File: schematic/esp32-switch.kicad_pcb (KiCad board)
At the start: 2 copper layers, 80 x 100 mm, 28 parts, among them J1 Direction, J11 Bouton 5v, J17 Bouton Batterie, J2 + - home, J3 a b x y, J4 L R ZL ZR, J5 Joy D, J6 Joy G, J7 Moteur vibration, Q1 BC547, U1 ESP32-DevKitC

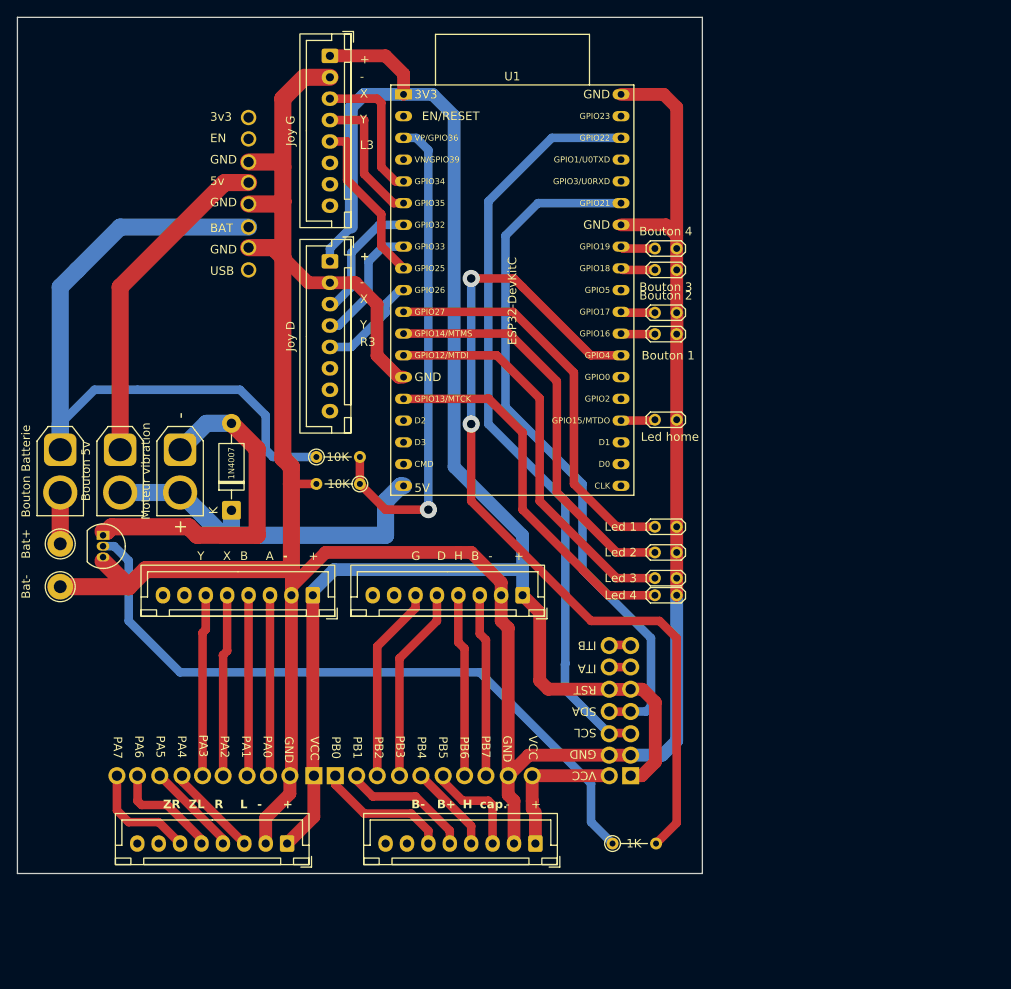
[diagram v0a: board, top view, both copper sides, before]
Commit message: changment des pates des leds
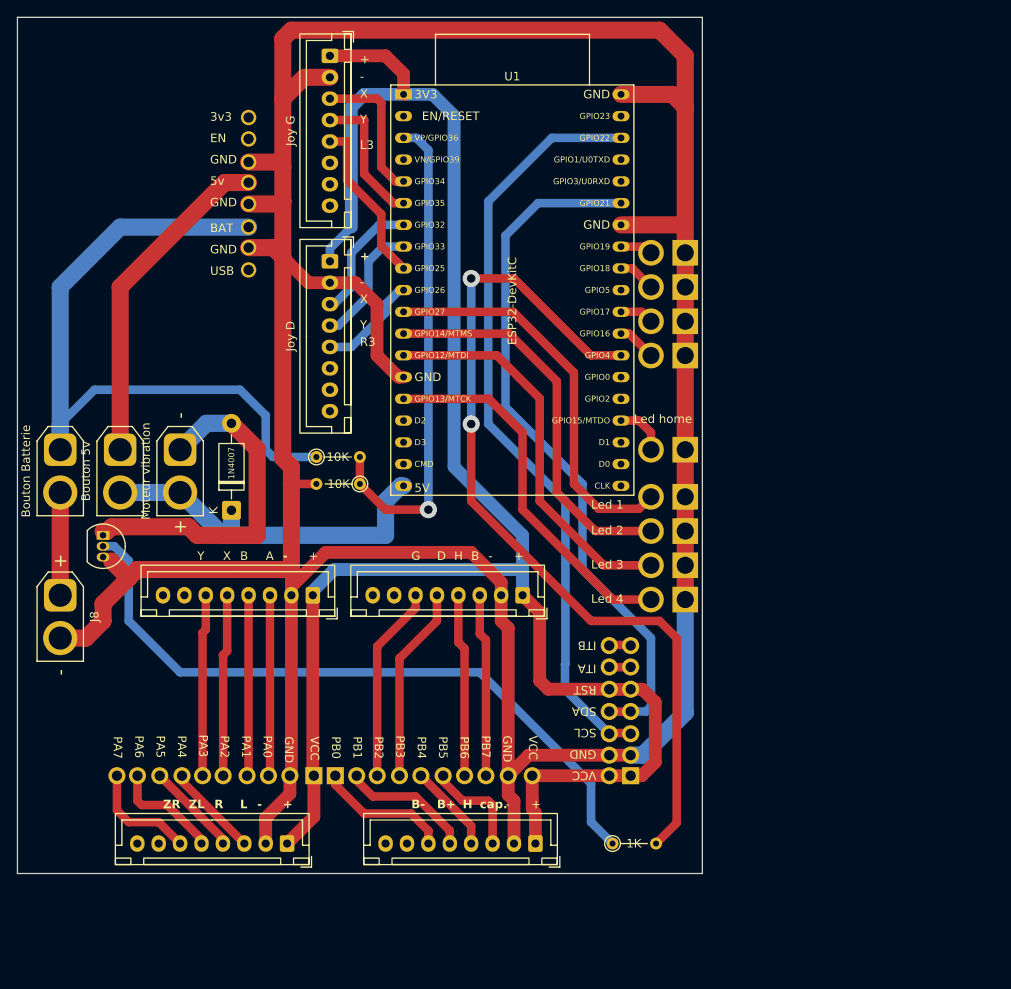
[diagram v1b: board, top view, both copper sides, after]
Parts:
- removed Bat+, Bat-: TestPoint_THTPad_D3.0mm_Drill1.5mm, TestPoint:TestPoint_THTPad_D3.0mm_Drill1.5mm
- removed JP1: Led 3, TestPoint:TestPoint_2Pads_Pitch2.54mm_Drill0.8mm
- removed JP2: Led 4, TestPoint:TestPoint_2Pads_Pitch2.54mm_Drill0.8mm
- removed JP3: Led 2, TestPoint:TestPoint_2Pads_Pitch2.54mm_Drill0.8mm
- removed JP4: Led home, TestPoint:TestPoint_2Pads_Pitch2.54mm_Drill0.8mm
- removed JP5: Led 1, TestPoint:TestPoint_2Pads_Pitch2.54mm_Drill0.8mm
- removed JP6: Bouton 1, TestPoint:TestPoint_2Pads_Pitch2.54mm_Drill0.8mm
- removed JP7: Bouton 2, TestPoint:TestPoint_2Pads_Pitch2.54mm_Drill0.8mm
- removed JP8: Bouton 3, TestPoint:TestPoint_2Pads_Pitch2.54mm_Drill0.8mm
- removed JP9: Bouton 4, TestPoint:TestPoint_2Pads_Pitch2.54mm_Drill0.8mm
- added J8: Batterie, Connector_AMASS:AMASS_XT30U-F_1x02_P5.0mm_Vertical, F.Cu at (133.0, 98.0)
- added Led1: Led 4, MyLibrary:Deux pads, F.Cu at (207.5, 97.0)
- added Led2: Led 2, MyLibrary:Deux pads, F.Cu at (207.5, 89.0)
- added Led3: Led 3, MyLibrary:Deux pads, F.Cu at (207.5, 93.0)
- added Led4: Led home, MyLibrary:Deux pads, F.Cu at (207.5, 79.5)
- added Led5: Led 1, MyLibrary:Deux pads, F.Cu at (207.5, 85.0)
- added Led6: Bouton 4, MyLibrary:Deux pads, F.Cu at (207.5, 56.5)
- added Led7: Bouton 3, MyLibrary:Deux pads, F.Cu at (207.5, 60.5)
- added Led8: Bouton 2, MyLibrary:Deux pads, F.Cu at (207.5, 64.5)
- added Led9: Bouton 1, MyLibrary:Deux pads, F.Cu at (207.5, 68.5)
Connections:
- J17 pad 2: unconnected-(J17-Pin_2-Pad2) -> Net-(J17-Pin_2)
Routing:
- net Net-(J1-Pin_2): track 308.6 -> 387.4 mm
- net Net-(J17-Pin_2): track 0.00 -> 12.0 mm
- net unconnected-(J17-Pin_2-Pad2): track 5.00 -> 0.00 mm
- net Net-(U1-MTDO/GPIO15/ADC2_CH3): track 3.79 -> 6.08 mm
- net Net-(J1-Pin_1): track 213.7 -> 215.5 mm
- net Net-(U1-MTMS/GPIO14/ADC2_CH6): track 47.6 -> 46.1 mm
- net Net-(U1-MTDI/GPIO12/ADC2_CH5): track 47.2 -> 46.1 mm
- net Net-(U1-ADC2_CH7/GPIO27): track 47.4 -> 46.6 mm
- net Net-(U1-GPIO16): track 3.98 -> 4.56 mm
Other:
- board text added: "Led 1"
- board text added: "Led 2"
- board text added: "Led 3"
- board text added: "Led 4"
- board text added: "Led home"

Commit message: changement de pcb
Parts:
- moved Q1 68.9 mm to (205.5, 105.0), turned to 0 degrees
- moved J1 60.8 mm to (234.5, 136.0)
- moved U2 57.4 mm to (187.0, 43.3), turned to -90 degrees
- moved J7 51.9 mm to (193.0, 105.0), turned to 0 degrees
- moved J3 44.7 mm to (186.0, 136.0)
- moved J11 39.8 mm to (179.0, 73.0), turned to 0 degrees
- moved D1 35.2 mm to (187.0, 97.0), turned to -90 degrees
- moved J5 34.8 mm to (194.0, 77.5)
- moved Led1 34.2 mm to (238.5, 111.5)
- moved J6 34.0 mm to (194.0, 52.0)
- moved Led3 33.1 mm to (238.5, 104.5)
- moved R2 32.6 mm to (144.0, 107.0), turned to -90 degrees
- moved Led2 32.1 mm to (238.5, 97.5)
- moved Led9 32.0 mm to (238.5, 76.5)
- moved Led5 31.5 mm to (238.5, 90.5)
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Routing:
- net Net-(J1-Pin_2): track 387.4 -> 528.0 mm
- net Net-(J1-Pin_1): track 215.5 -> 298.5 mm
- net Net-(Q1-B): track 80.6 -> 8.49 mm
- net Net-(U1-ADC2_CH0/GPIO4): track 102.8 -> 46.1 mm, vias 2 -> 1
- net Net-(U1-SENSOR_VP/GPIO36/ADC1_CH0): track 57.9 -> 111.7 mm, vias 1 -> 0
- net Net-(J17-Pin_1): track 84.1 -> 47.6 mm
- net Net-(J11-Pin_1): track 39.1 -> 11.5 mm
- net Net-(U1-GPIO21): track 82.2 -> 63.4 mm, vias 0 -> 1
- net Net-(D1-A): track 40.2 -> 25.1 mm
- net Net-(U1-GPIO22): track 89.1 -> 74.5 mm, vias 0 -> 1
- net Net-(U1-GPIO19): track 3.80 -> 18.0 mm
- net Net-(J1-Pin_6): track 22.9 -> 37.1 mm
- net Net-(J1-Pin_5): track 22.9 -> 36.8 mm
- net Net-(J5-Pin_5): track 11.5 -> 24.4 mm
- net Net-(U1-ADC2_CH7/GPIO27): track 46.6 -> 56.8 mm
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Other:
- board size 80 x 100 mm -> 100 x 100 mm
- board text removed: "+"
- board text removed: "-"
- board text removed: "A"
- board text removed: "B"
- board text removed: "B+"
- board text removed: "B-"
- board text removed: "D"
- board text removed: "G"
- board text removed: "H"
- board text removed: "L"
- board text removed: "L3"
- board text removed: "Led 1"
- board text removed: "Led 2"
- board text removed: "Led 3"
- board text removed: "Led 4"
- board text removed: "Led home"
- board text removed: "R"
- board text removed: "R3"
- board text removed: "X"
- board text removed: "Y"
- board text removed: "ZL"
- board text removed: "ZR"
- board text removed: "cap."

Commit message: mise à jour du pcb
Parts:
- moved U2 63.8 mm to (182.5, 107.0), turned to 180 degrees
- moved J11 14.8 mm to (186.0, 86.0), turned to -90 degrees
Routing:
- net Net-(J1-Pin_2): track 528.0 -> 574.2 mm
- net Net-(J17-Pin_1): track 47.6 -> 23.2 mm
- net Net-(D1-K): track 49.4 -> 30.6 mm
- net Net-(J11-Pin_1): track 11.5 -> 29.8 mm
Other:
- board text added: "+"

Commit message: Mise à jour du pcb
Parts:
- moved J1 99.1 mm to (182.0, 52.0), turned to -90 degrees
- moved U3 89.1 mm to (156.9, 49.0), turned to 0 degrees
- moved J3 75.1 mm to (153.0, 68.5), turned to -90 degrees
- moved J2 62.8 mm to (182.0, 80.0), turned to -90 degrees
- moved J17 56.1 mm to (192.0, 122.0), turned to 180 degrees
- moved U2 55.4 mm to (237.4, 114.3), turned to -90 degrees
- moved J8 54.8 mm to (187.0, 114.0)
- moved R2 49.0 mm to (188.0, 85.5), turned to 90 degrees
- moved J11 45.4 mm to (224.5, 110.0), turned to 180 degrees
- moved R1 44.3 mm to (188.0, 93.5), turned to 90 degrees
- moved J4 42.9 mm to (153.0, 94.0), turned to -90 degrees
- moved J7 17.6 mm to (210.0, 109.5), turned to 90 degrees
- moved R3 9.02 mm to (203.0, 106.5)
- moved D1 8.91 mm to (195.0, 100.9)
- moved Q1 8.76 mm to (201.0, 112.5), turned to 90 degrees
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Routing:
- net Net-(J1-Pin_2): track 574.2 -> 513.6 mm
- net Net-(J1-Pin_1): track 298.5 -> 245.1 mm
- net Net-(U1-SENSOR_VP/GPIO36/ADC1_CH0): track 111.7 -> 67.8 mm
- net Net-(J17-Pin_1): track 23.2 -> 63.0 mm
- net Net-(J3-Pin_6): track 11.4 -> 35.6 mm
- net Net-(J3-Pin_4): track 11.3 -> 35.5 mm
- net Net-(J3-Pin_5): track 11.5 -> 35.6 mm
- net Net-(J3-Pin_3): track 11.3 -> 34.9 mm
- net Net-(U1-GPIO21): track 63.4 -> 84.7 mm, vias 1 -> 0
- net Net-(J1-Pin_5): track 36.8 -> 21.5 mm
- net Net-(U1-ADC2_CH0/GPIO4): track 46.1 -> 31.7 mm
- net Net-(J1-Pin_4): track 30.8 -> 16.7 mm
- net Net-(J1-Pin_3): track 30.8 -> 17.0 mm
- net Net-(J1-Pin_6): track 37.1 -> 24.7 mm
- net Net-(D1-K): track 30.6 -> 41.2 mm
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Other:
- board text added: "Joy D"
- board text removed: "+"

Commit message: Ajout de texte
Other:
- board text added: "BDI"
- board text added: "BDS"
- board text added: "BGI"
- board text added: "BGS"
- board text added: "L1"
- board text added: "L2"
- board text added: "L3"
- board text added: "L4"
- board text added: "LH"
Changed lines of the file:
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@@
 		(layer "Edge.Cuts")
+	)
+	(gr_text "LH"
+		(at 229 80 0)
+		(layer "F.SilkS")
+		(effects
+			(font
+				(size 1 1)
+				(thickness 0.1)
+			)
+			(justify left bottom)
+		)
+	)
+	(gr_text "BDI"
+		(at 228 58 0)
+		(layer "F.SilkS")
+		(effects
+			(font
+				(size 1 1)
+				(thickness 0.1)
+			)
+			(justify left bottom)
+		)
+	)
+	(gr_text "L4"
+		(at 229 107 0)
+		(layer "F.SilkS")
+		(effects
+			(font
+				(size 1 1)
+				(thickness 0.1)
+			)
+			(justify left bottom)
+		)
 	)
 	(gr_text "Joy D"
@@
 		)
 	)
+	(gr_text "L1"
+		(at 229 85 0)
+		(layer "F.SilkS")
+		(effects
+			(font
+				(size 1 1)
+				(thickness 0.1)
+			)
+			(justify left bottom)
+		)
+	)
+	(gr_text "L3"
+		(at 229 103 0)
+		(layer "F.SilkS")
+		(effects
+			(font
+				(size 1 1)
+				(thickness 0.1)
+			)
+			(justify left bottom)
+		)
+	)
+	(gr_text "BGS"
+		(at 228 74 0)
+		(layer "F.SilkS")
+		(effects
+			(font
+				(size 1 1)
+				(thickness 0.1)
+			)
+			(justify left bottom)
+		)
+	)
+	(gr_text "L2"
+		(at 229 94 0)
+		(layer "F.SilkS")
+		(effects
+			(font
+				(size 1 1)
+				(thickness 0.1)
+			)
+			(justify left bottom)
+		)
+	)
+	(gr_text "BDS"
+		(at 228 62 0)
+		(layer "F.SilkS")
+		(effects
+			(font
+				(size 1 1)
+				(thickness 0.1)
+			)
+			(justify left bottom)
+		)
+	)
+	(gr_text "BGI"
+		(at 228 69 0)
+		(layer "F.SilkS")
+		(effects
+			(font
+				(size 1 1)
+				(thickness 0.1)
+			)
+			(justify left bottom)
+		)
+	)
